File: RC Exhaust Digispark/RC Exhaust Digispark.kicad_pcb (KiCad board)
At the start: 2 copper layers, 25.2 x 29.2 mm, 12 parts, among them J5 THR, J6 THR_Y

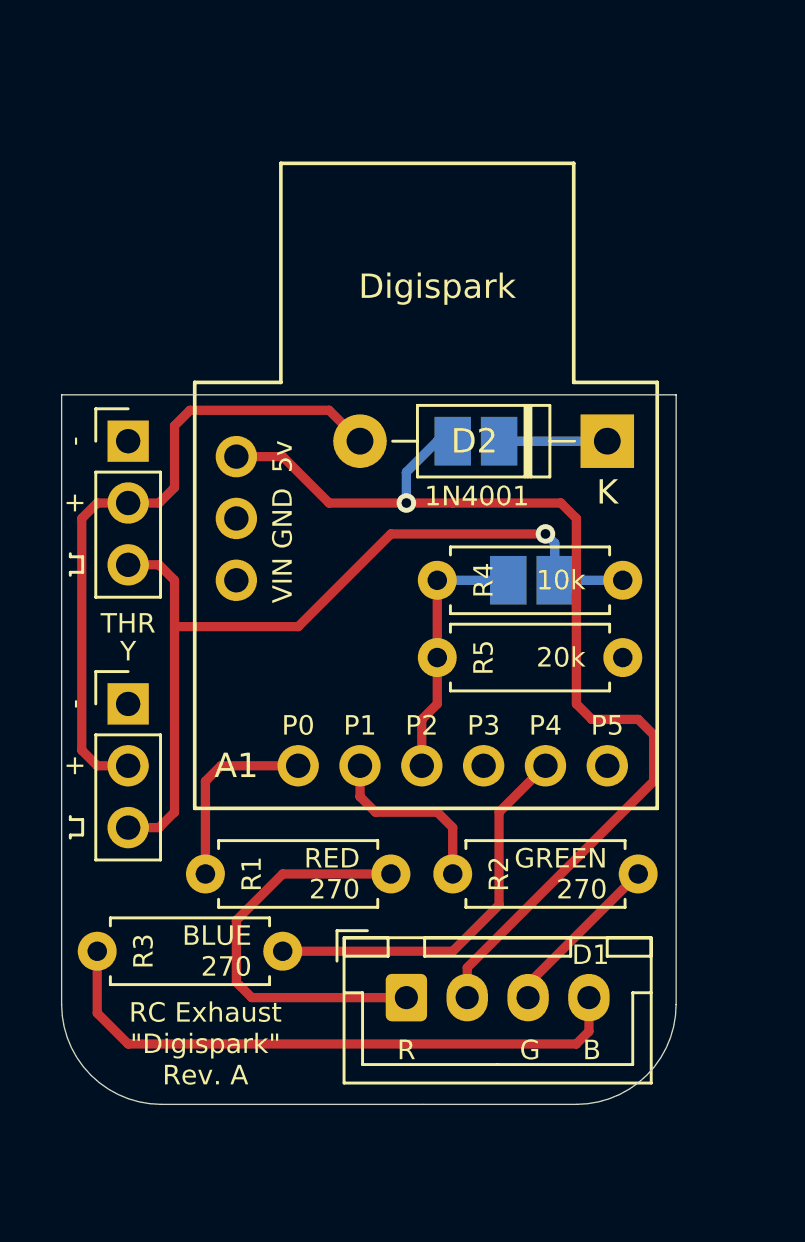
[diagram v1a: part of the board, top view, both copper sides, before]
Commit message: Small exhaust tweaks to better fit Digistump into computers
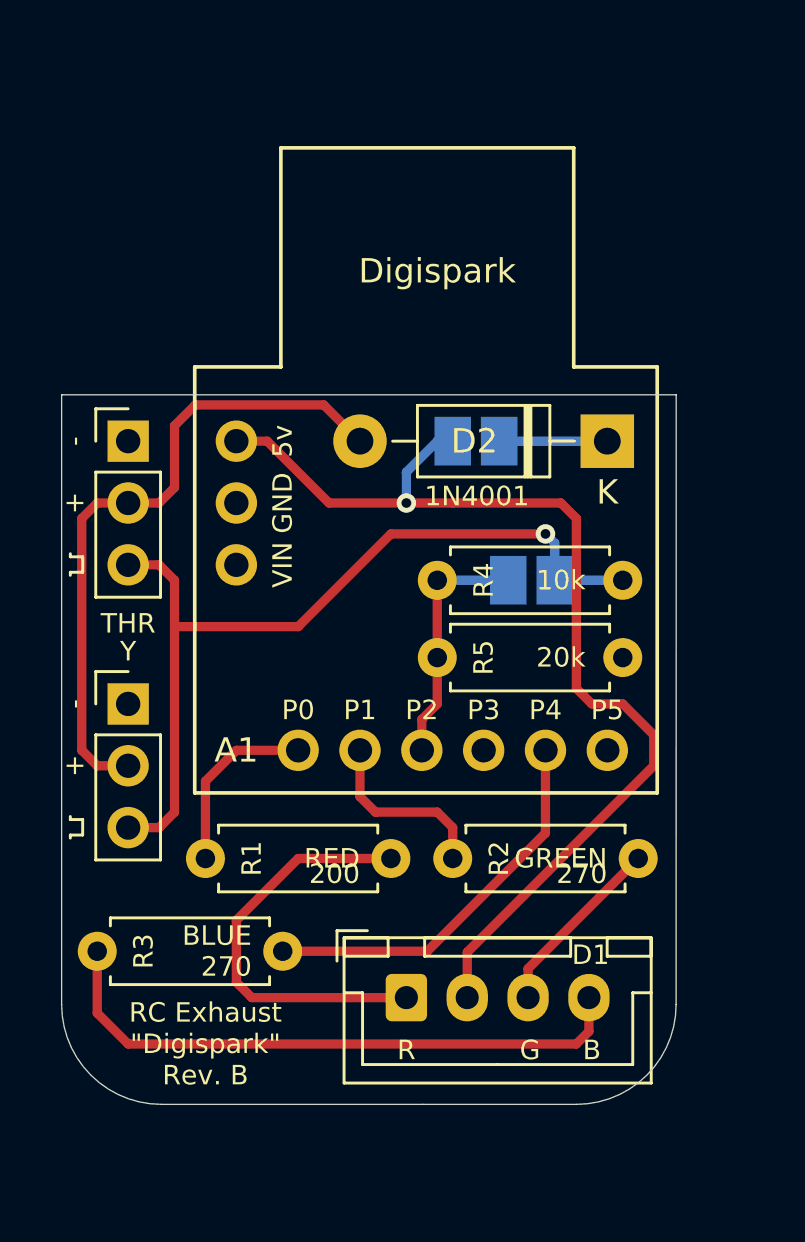
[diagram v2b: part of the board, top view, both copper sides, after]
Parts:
- R1: value 270 -> 200
- moved R1 0.64 mm to (113.7, 96.5)
- moved R2 0.64 mm to (123.8, 96.5)
- moved A1 0.63 mm to (122.6, 92.1)
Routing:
- net Net-(D1-Pad3): track 6.95 -> 7.59 mm
- net THR: track 10.8 -> 10.2 mm
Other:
- board text added: "RC Exhaust "Digispark" Rev. B"
- board text removed: "RC Exhaust "Digispark" Rev. A"
